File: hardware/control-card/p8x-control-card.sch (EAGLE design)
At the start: 34 parts, among them J1 DIN41612-96M, U1 CLK DIV, U10 UCODE ROM0, U11 UCODE ROM1, U12 UCODE ROM2, U13 UCODE ROM3, U14 PIPE0, U15 PIPE1, U16 PIPE2, U17 PIPE3, U18 STEP CNT, U2 74HCT14, U3 74HCT74, U4 74HCT00, U5 74HCT08, U6 74HCT32, U7 IR 74HCT377, U8 DLD DEC, U9 COND MUX, X1 4MHZ

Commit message: hw(rev B): control card — pipeline latches remapped to rev-B word
Phase 2, step 2. The 4x 74374 pipeline latches now map the 32-bit rev-B
control word: U15 gains PSEL2 (3-bit pointer select), ALUS3 moves to
U16, and U17 drives FCOND2/URST/HALT plus the new LDZN/SHCIN/SETC/CLRC.
The control card now drives PSEL2 (to reg-bank) and LDZN/SHCIN/SETC/CLRC
(to ALU) onto the backplane. Card retitled REV B; schematic regenerated,
validates clean.

Co-Authored-By: Claude Opus 4.8 <noreply@anthropic.com>
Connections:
- new net CLRC: J1.B27, U17.Q7
- new net LDZN: J1.C28, U17.Q4
- new net P17B2: U13.IO2, U17.D3
- new net P17B3: U13.IO3, U17.D4
- new net P17B4: U13.IO4, U17.D5
- new net P17B5: U13.IO5, U17.D6
- new net P17B6: U13.IO6, U17.D7
- new net PSEL2: J1.C27, U15.Q3
- new net SETC: J1.C30, U17.Q6
- new net SHCIN: J1.C29, U17.Q5
- net ALUM: now also U16.Q2; no longer U16.Q1
- net ALUS0: now also U15.Q6; no longer U15.Q5
- net ALUS1: now also U15.Q7; no longer U15.Q6
- net ALUS2: now also U15.Q8; no longer U15.Q7
- net ALUS3: now also U16.Q1; no longer U15.Q8
- net CIN: now also U16.Q3; no longer U16.Q2
- net FCOND0: now also U16.Q7; no longer U16.Q6
- net FCOND1: now also U16.Q8; no longer U16.Q7
- net FCOND2: now also U17.Q1; no longer U16.Q8
- net HALT: now also U17.Q3; no longer U17.Q2
- net LDF: now also U16.Q6; no longer U16.Q5
- net PDEC: now also U15.Q5; no longer U15.Q4
- net PINC: now also U15.Q4; no longer U15.Q3
- net SH0: now also U16.Q4; no longer U16.Q3
- net SH1: now also U16.Q5; no longer U16.Q4
- net URST: now also U17.Q2; no longer U17.Q1
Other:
- note added: "P8X CONTROL/MICROCODE CARD REV B"
- note removed: "P8X CONTROL/MICROCODE CARD REV A"

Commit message: hw: per-IC 100nF decoupling caps on every card
card standards sec.5 requires a decoupling cap per IC; only the backplane had
them. gen_eagle's card() now generates one 100nF cap (CDn, C_DISC footprint)
per IC on the five plug-in cards, placed next to its IC and wired VCC<->GND;
the memory card's separate build does the same for U1-U9.

Caps added: control 18, regbank 44, alu 31, io 15, cf 8, memory 9. All 7
boards regenerate with 0 validation errors; card schematic PDFs refreshed.
Placement is approximate (caps sit just below each IC) pending Fusion routing.

Clears a pre-fab blocker from the backlog.

Co-Authored-By: Claude Opus 4.8 <noreply@anthropic.com>
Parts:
- added CD1, CD10, CD11, CD12, CD13, CD14, CD15, CD16, CD17, CD18, CD2, CD3, CD4, CD5, CD6, CD7, CD8, CD9: 100N, p8x:CAP
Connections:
- net GND: now also CD1.2, CD10.2, CD11.2, CD12.2, CD13.2, CD14.2, CD15.2, CD16.2, CD17.2, CD18.2, CD2.2, CD3.2, CD4.2, CD5.2, CD6.2, CD7.2, CD8.2, CD9.2
- net VCC: now also CD1.1, CD10.1, CD11.1, CD12.1, CD13.1, CD14.1, CD15.1, CD16.1, CD17.1, CD18.1, CD2.1, CD3.1, CD4.1, CD5.1, CD6.1, CD7.1, CD8.1, CD9.1

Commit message: feat: 2nd ALU-input mux (rev C) — B-side operand can select T
Add a 2:1 mux on the ALU B-operand path so the second ALU operand can be
the T register instead of B, controlled by a new microcode-word bit.

- microcode (genucode.py): BSEL = word bit 31 (was the lone spare); new
  opcodes ADDT/SUBT/ANDT/ORT/XORT/CMPT (0x80-0x85) run the ALU with T as
  the B operand (B preserved); LDT #imm / LDT a (0x86/0x87) expose T, which
  was microcode-scratch-only and had no programmer-visible load.
- emulator (p8xemu.c): decode bit 31; ALU B operand = bsel ? T : B.
- hardware (gen_eagle.py): ALU card U32/U33 (74157 x2) mux BQ vs TQ -> 74181 B;
  BSEL latched in control-card pipe U17.Q8, carried on backplane B28 (was
  SPARE9). All 7 boards regenerate with 0 validation errors.
- bus map kept consistent across both generators (gen_eagle.py, gen_bus_pdf.py),
  the backplane render, and the hardware docs (bus-definition is authoritative).
- tests: new ISA coverage for the T-operand ops (sentinel wrong-operand bait);
  all 6 suites pass.
- docs: programmer's guide regenerated; BACKLOG updated (mux -> DONE; added a
  post-bringup idea to optimize monitor/OS/BASIC hot paths with the T ops).

Backward-compatible: no existing opcode changed; BSEL defaults 0 (= B register),
so existing monitor/OS/BASIC binaries are byte-identical.

Co-Authored-By: Claude Opus 4.8 <noreply@anthropic.com>
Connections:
- new net BSEL: J1.B28, U17.Q8
- new net P17B7: U13.IO7, U17.D8
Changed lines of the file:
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@@
 <label x="-22.86" y="-108.71" size="1.778" layer="95"/></segment>
+</net>
+<net name="P17B7" class="0">
+<segment><pinref part="U17" gate="G$1" pin="D8"/>
+<wire x1="122.22" y1="-543.56" x2="117.14" y2="-543.56" width="0.1524" layer="91"/>
+<label x="117.14" y="-543.05" size="1.778" layer="95"/></segment>
+<segment><pinref part="U13" gate="G$1" pin="IO7"/>
+<wire x1="157.78" y1="-398.78" x2="162.86" y2="-398.78" width="0.1524" layer="91"/>
+<label x="162.86" y="-398.27" size="1.778" layer="95"/></segment>
+</net>
+<net name="BSEL" class="0">
+<segment><pinref part="U17" gate="G$1" pin="Q8"/>
+<wire x1="157.78" y1="-538.48" x2="162.86" y2="-538.48" width="0.1524" layer="91"/>
+<label x="162.86" y="-537.97" size="1.778" layer="95"/></segment>
+<segment><pinref part="J1" gate="G$1" pin="B28"/>
+<wire x1="-17.78" y1="-111.76" x2="-22.86" y2="-111.76" width="0.1524" layer="91"/>
+<label x="-22.86" y="-111.25" size="1.778" layer="95"/></segment>
 </net>
 <net name="-USTL" class="0">

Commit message: feat: V flag + signed comparison branches (rev C)
Implement signed overflow (V) and signed-compare branches end to end, so the
machine can do signed ordering (C alone only gives unsigned).

Hardware (the old "one 7486 from carry-in vs carry-out of bit 7" plan was not
feasible: a 74181 4-bit group doesn't expose carry-into-bit-7). Sign-bit method:
  V = (A7 ^ F7) & (A7 ^ B7 ^ ~ALUS2)
  (B7 = muxed B operand, F7 = raw ALU result sign; isADD = ~S2). Ungated by M,
  so V is valid after ADD/SUB/CMP.
- ALU card: U34 (74HCT86) + U35 (74HCT08) derive V into the flag register
  (was tied low). FV already bused, no bus change.
- control card: U19 (74HCT86) -> N^V on cond-mux D6; spare U6 OR gate ->
  (N^V)|Z on D7 (both were grounded). FCOND 6/7 select them.

Microcode: BLT/BGE/BLE/BGT (0x44-0x47), FC LT=6 (N^V), LE=7 ((N^V)|Z).
Emulator: computes V by the identical Boolean; cond cases 6/7 added.
Tests: ISA coverage for sign-boundary cases unsigned C gets wrong (e.g. -128<1).
Docs: programmer's guide + BACKLOG (V flag VERIFY -> DONE).

All 7 boards regenerate with 0 validation errors; all 6 test suites pass.

Co-Authored-By: Claude Opus 4.8 <noreply@anthropic.com>
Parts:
- added CD19: 100N, p8x:CAP
- added U19: 74HCT86 NV-XOR, p8x:GATES14
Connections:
- new net NV: U19.1Y, U6.4A, U9.D6
- new net NVZ: U6.4Y, U9.D7
- net FN: now also U19.1A
- net FV: now also U19.1B
- net FZ: now also U6.4B
- net GND: now also CD19.2, U19.2A, U19.2B, U19.3A, U19.3B, U19.4A, U19.4B; no longer U6.4A, U6.4B, U9.D6, U9.D7
- net VCC: now also CD19.1
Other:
- moved on the sheet: C1, CD1, CD10, CD11, CD12, CD13, CD14, CD15, CD16, CD17, CD18, CD2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

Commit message: feat(hw): provision IRQ controller footprints (DNP) + reserve IRQ bus line
Per the chosen conservative path: add the interrupt-controller footprints and
the IRQ bus line so the controller can be built post-fab without a respin, but
WITHOUT the bus-critical logic that could brick an unvalidated board.

- Control card: U20 (74244 forcing buffer) + U21 (7474 IE/pending FF) placed as
  DNP. Safe connections wired: U20 inputs = $08 pattern, U20 !G tied high
  (outputs forced high-Z), IRQ line -> U21. Left UNWIRED (bus-critical, design
  with DRC first): U20 outputs onto the data bus, the enable/service sequencer,
  the EI/DI/RTI opcode decode, and the cross-card memory -RD suppression.
- Backplane: B29 = IRQ (was SPARE10), reserved; SPARE11 remains on B30.
- Bus map kept consistent across both generators + the backplane render + the
  three hardware docs (bus-definition is authoritative). Programmer's guide and
  BACKLOG updated.

All 7 boards regenerate with 0 validation errors; all 6 test suites pass.

Co-Authored-By: Claude Opus 4.8 <noreply@anthropic.com>
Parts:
- added CD20, CD21: 100N, p8x:CAP
- added U20: IRQ-FORCE DNP, p8x:74244
- added U21: IRQ/IE FF DNP, p8x:7474
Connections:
- new net IRQ: J1.B29, U21.1D
- net -RES: now also U21.!1CLR, U21.!2CLR
- net GND: now also CD20.2, CD21.2, U20.A1, U20.A2, U20.A3, U20.A5, U20.A6, U20.A7, U20.A8, U21.1CLK, U21.2CLK, U21.2D
- net VCC: now also CD20.1, CD21.1, U20.!G1, U20.!G2, U20.A4, U21.!1PRE, U21.!2PRE
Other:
- moved on the sheet: C1, CD1, CD10, CD11, CD12, CD13, CD14, CD15, CD16, CD17, CD18, CD19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

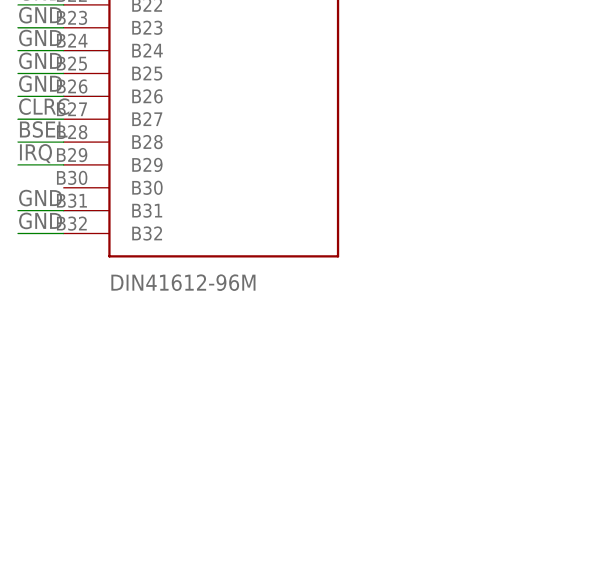
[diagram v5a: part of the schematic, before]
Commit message: fix(bom): card DIN connectors were undercounted (1 -> 6); label them FABC96R
Two fixes:
- card() built CARDS[name] from `allp`, which omitted J1 — so the 5 plug-in
  cards' DIN41612 edge connectors never reached the BOM (it showed qty 1, only
  the memory card's J1). Include J1 in allp (the schematic renderer already
  filters J1 by name, so rendering is unchanged). BOM now correctly shows 6 card
  connectors + 10 backplane receptacles.
- Card edge connector is FABC96R (user-specified): set the value label on every
  card J1 and name it in the BOM; backplane receptacles noted as the mating part.

Regenerated all boards + PDFs + BOM; all 6 test suites pass.

Co-Authored-By: Claude Opus 4.8 <noreply@anthropic.com>
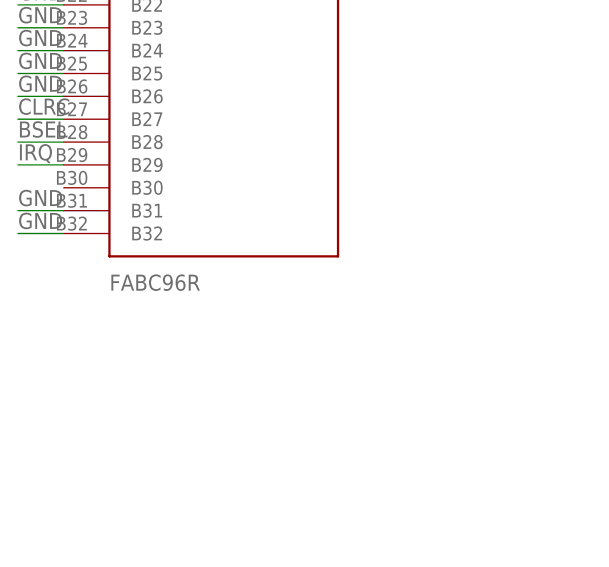
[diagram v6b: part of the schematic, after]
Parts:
- J1: value DIN41612-96M -> FABC96R
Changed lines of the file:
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@@
 <classes><class number="0" name="default" width="0" drill="0"/></classes>
 <parts>
-<part name="J1" library="p8x" deviceset="DIN96" device="" value="DIN41612-96M"/>
+<part name="J1" library="p8x" deviceset="DIN96" device="" value="FABC96R"/>
 <part name="U1" library="p8x" deviceset="74161" device="" value="CLK DIV"/>
 <part name="U2" library="p8x" deviceset="HEX14" device="" value="74HCT14"/>

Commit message: fix(hardware): connect IC power pins on the card()-built boards
Schematic-review fix. card() wired the edge-connector and decoupling-cap pins to
VCC/GND but never added each IC's own VCC/GND supply pin, so on control, regbank,
ALU, I/O, and CF the chips' power pads were not members of the power pours and
would not have been powered. (The hand-built memory card already did this; the
backplane has no ICs. validate() couldn't catch it — it checks pin-name legality,
not connectivity.)

- card(): append (ref,"VCC")/(ref,"GND") for every IC, skipping any pin already
  wired by hand (idempotent — avoids duplicate pinrefs, e.g. ALU U16 GND)
- regenerated all 7 boards (.sch/.brd), 0 validation errors
- board-level audit: every IC on every card now has both VCC and GND on the
  power signals
- BACKLOG: moved the critical item to DONE; theory docs' power-pin callouts
  updated to "fixed"

Co-Authored-By: Claude Opus 4.8 <noreply@anthropic.com>
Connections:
- net GND: now also U1.GND, U10.GND, U11.GND, U12.GND, U13.GND, U14.GND, U15.GND, U16.GND, U17.GND, U18.GND, U19.GND, U2.GND, U20.GND, U21.GND, U3.GND, U4.GND, U5.GND, U6.GND, U7.GND, U8.GND, U9.GND
- net VCC: now also U1.VCC, U10.VCC, U11.VCC, U12.VCC, U13.VCC, U14.VCC, U15.VCC, U16.VCC, U17.VCC, U18.VCC, U19.VCC, U2.VCC, U20.VCC, U21.VCC, U3.VCC, U4.VCC, U5.VCC, U6.VCC, U7.VCC, U8.VCC, U9.VCC
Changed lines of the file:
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@@
 <wire x1="122.22" y1="-1917.70" x2="117.14" y2="-1917.70" width="0.1524" layer="91"/>
 <label x="117.14" y="-1917.19" size="1.778" layer="95"/></segment>
+<segment><pinref part="U1" gate="G$1" pin="VCC"/>
+<wire x1="157.78" y1="25.40" x2="162.86" y2="25.40" width="0.1524" layer="91"/>
+<label x="162.86" y="25.91" size="1.778" layer="95"/></segment>
+<segment><pinref part="U2" gate="G$1" pin="VCC"/>
+<wire x1="259.38" y1="22.86" x2="264.46" y2="22.86" width="0.1524" layer="91"/>
+<label x="264.46" y="23.37" size="1.778" layer="95"/></segment>
+<segment><pinref part="U3" gate="G$1" pin="VCC"/>
+<wire x1="360.98" y1="27.94" x2="366.06" y2="27.94" width="0.1524" layer="91"/>
+<label x="366.06" y="28.45" size="1.778" layer="95"/></segment>
+<segment><pinref part="U4" gate="G$1" pin="VCC"/>
+<wire x1="462.58" y1="27.94" x2="467.66" y2="27.94" width="0.1524" layer="91"/>
+<label x="467.66" y="28.45" size="1.778" layer="95"/></segment>
+<segment><pinref part="U5" gate="G$1" pin="VCC"/>
+<wire x1="157.78" y1="-111.76" x2="162.86" y2="-111.76" width="0.1524" layer="91"/>
+<label x="162.86" y="-111.25" size="1.778" layer="95"/></segment>
+<segment><pinref part="U6" gate="G$1" pin="VCC"/>
+<wire x1="259.38" y1="-111.76" x2="264.46" y2="-111.76" width="0.1524" layer="91"/>
+<label x="264.46" y="-111.25" size="1.778" layer="95"/></segment>
+<segment><pinref part="U7" gate="G$1" pin="VCC"/>
+<wire x1="360.98" y1="-121.92" x2="366.06" y2="-121.92" width="0.1524" layer="91"/>
+<label x="366.06" y="-121.41" size="1.778" layer="95"/></segment>
+<segment><pinref part="U8" gate="G$1" pin="VCC"/>
+<wire x1="462.58" y1="-121.92" x2="467.66" y2="-121.92" width="0.1524" layer="91"/>
+<label x="467.66" y="-121.41" size="1.778" layer="95"/></segment>
+<segment><pinref part="U9" gate="G$1" pin="VCC"/>
+<wire x1="157.78" y1="-246.38" x2="162.86" y2="-246.38" width="0.1524" layer="91"/>
+<label x="162.86" y="-245.87" size="1.778" layer="95"/></segment>
+<segment><pinref part="U10" gate="G$1" pin="VCC"/>
+<wire x1="259.38" y1="-274.32" x2="264.46" y2="-274.32" width="0.1524" layer="91"/>
+<label x="264.46" y="-273.81" size="1.778" layer="95"/></segment>
+<segment><pinref part="U11" gate="G$1" pin="VCC"/>
+<wire x1="360.98" y1="-274.32" x2="366.06" y2="-274.32" width="0.1524" layer="91"/>
+<label x="366.06" y="-273.81" size="1.778" layer="95"/></segment>
+<segment><pinref part="U12" gate="G$1" pin="VCC"/>
+<wire x1="462.58" y1="-274.32" x2="467.66" y2="-274.32" width="0.1524" layer="91"/>
+<label x="467.66" y="-273.81" size="1.778" layer="95"/></segment>
+<segment><pinref part="U13" gate="G$1" pin="VCC"/>
+<wire x1="157.78" y1="-414.02" x2="162.86" y2="-414.02" width="0.1524" layer="91"/>
+<label x="162.86" y="-413.51" size="1.778" layer="95"/></segment>
+<segment><pinref part="U14" gate="G$1" pin="VCC"/>
+<wire x1="259.38" y1="-401.32" x2="264.46" y2="-401.32" width="0.1524" layer="91"/>
+<label x="264.46" y="-400.81" size="1.778" layer="95"/></segment>
+<segment><pinref part="U15" gate="G$1" pin="VCC"/>
+<wire x1="360.98" y1="-401.32" x2="366.06" y2="-401.32" width="0.1524" layer="91"/>
+<label x="366.06" y="-400.81" size="1.778" layer="95"/></segment>
+<segment><pinref part="U16" gate="G$1" pin="VCC"/>
+<wire x1="462.58" y1="-401.32" x2="467.66" y2="-401.32" width="0.1524" layer="91"/>
+<label x="467.66" y="-400.81" size="1.778" layer="95"/></segment>
+<segment><pinref part="U17" gate="G$1" pin="VCC"/>
+<wire x1="157.78" y1="-541.02" x2="162.86" y2="-541.02" width="0.1524" layer="91"/>
+<label x="162.86" y="-540.51" size="1.778" layer="95"/></segment>
+<segment><pinref part="U18" gate="G$1" pin="VCC"/>
+<wire x1="259.38" y1="-533.40" x2="264.46" y2="-533.40" width="0.1524" layer="91"/>
+<label x="264.46" y="-532.89" size="1.778" layer="95"/></segment>
+<segment><pinref part="U19" gate="G$1" pin="VCC"/>
+<wire x1="360.98" y1="-530.86" x2="366.06" y2="-530.86" width="0.1524" layer="91"/>
+<label x="366.06" y="-530.35" size="1.778" layer="95"/></segment>
+<segment><pinref part="U20" gate="G$1" pin="VCC"/>
+<wire x1="462.58" y1="-541.02" x2="467.66" y2="-541.02" width="0.1524" layer="91"/>
+<label x="467.66" y="-540.51" size="1.778" layer="95"/></segment>
+<segment><pinref part="U21" gate="G$1" pin="VCC"/>
+<wire x1="157.78" y1="-670.56" x2="162.86" y2="-670.56" width="0.1524" layer="91"/>
+<label x="162.86" y="-670.05" size="1.778" layer="95"/></segment>
 </net>
 <net name="GND" class="0">
@@
 <wire x1="157.78" y1="-1917.70" x2="162.86" y2="-1917.70" width="0.1524" layer="91"/>
 <label x="162.86" y="-1917.19" size="1.778" layer="95"/></segment>
+<segment><pinref part="U1" gate="G$1" pin="GND"/>
+<wire x1="157.78" y1="22.86" x2="162.86" y2="22.86" width="0.1524" layer="91"/>
+<label x="162.86" y="23.37" size="1.778" layer="95"/></segment>
+<segment><pinref part="U2" gate="G$1" pin="GND"/>
+<wire x1="259.38" y1="20.32" x2="264.46" y2="20.32" width="0.1524" layer="91"/>
+<label x="264.46" y="20.83" size="1.778" layer="95"/></segment>
+<segment><pinref part="U3" gate="G$1" pin="GND"/>
+<wire x1="360.98" y1="25.40" x2="366.06" y2="25.40" width="0.1524" layer="91"/>
+<label x="366.06" y="25.91" size="1.778" layer="95"/></segment>
+<segment><pinref part="U4" gate="G$1" pin="GND"/>
+<wire x1="462.58" y1="25.40" x2="467.66" y2="25.40" width="0.1524" layer="91"/>
+<label x="467.66" y="25.91" size="1.778" layer="95"/></segment>
+<segment><pinref part="U5" gate="G$1" pin="GND"/>
+<wire x1="157.78" y1="-114.30" x2="162.86" y2="-114.30" width="0.1524" layer="91"/>
+<label x="162.86" y="-113.79" size="1.778" layer="95"/></segment>
+<segment><pinref part="U6" gate="G$1" pin="GND"/>
+<wire x1="259.38" y1="-114.30" x2="264.46" y2="-114.30" width="0.1524" layer="91"/>
+<label x="264.46" y="-113.79" size="1.778" layer="95"/></segment>
+<segment><pinref part="U7" gate="G$1" pin="GND"/>
+<wire x1="360.98" y1="-124.46" x2="366.06" y2="-124.46" width="0.1524" layer="91"/>
+<label x="366.06" y="-123.95" size="1.778" layer="95"/></segment>
+<segment><pinref part="U8" gate="G$1" pin="GND"/>
+<wire x1="462.58" y1="-124.46" x2="467.66" y2="-124.46" width="0.1524" layer="91"/>
+<label x="467.66" y="-123.95" size="1.778" layer="95"/></segment>
+<segment><pinref part="U9" gate="G$1" pin="GND"/>
+<wire x1="157.78" y1="-248.92" x2="162.86" y2="-248.92" width="0.1524" layer="91"/>
+<label x="162.86" y="-248.41" size="1.778" layer="95"/></segment>
+<segment><pinref part="U10" gate="G$1" pin="GND"/>
+<wire x1="259.38" y1="-276.86" x2="264.46" y2="-276.86" width="0.1524" layer="91"/>
+<label x="264.46" y="-276.35" size="1.778" layer="95"/></segment>
+<segment><pinref part="U11" gate="G$1" pin="GND"/>
+<wire x1="360.98" y1="-276.86" x2="366.06" y2="-276.86" width="0.1524" layer="91"/>
+<label x="366.06" y="-276.35" size="1.778" layer="95"/></segment>
+<segment><pinref part="U12" gate="G$1" pin="GND"/>
+<wire x1="462.58" y1="-276.86" x2="467.66" y2="-276.86" width="0.1524" layer="91"/>
+<label x="467.66" y="-276.35" size="1.778" layer="95"/></segment>
+<segment><pinref part="U13" gate="G$1" pin="GND"/>
+<wire x1="157.78" y1="-416.56" x2="162.86" y2="-416.56" width="0.1524" layer="91"/>
+<label x="162.86" y="-416.05" size="1.778" layer="95"/></segment>
+<segment><pinref part="U14" gate="G$1" pin="GND"/>
+<wire x1="259.38" y1="-403.86" x2="264.46" y2="-403.86" width="0.1524" layer="91"/>
+<label x="264.46" y="-403.35" size="1.778" layer="95"/></segment>
+<segment><pinref part="U15" gate="G$1" pin="GND"/>
+<wire x1="360.98" y1="-403.86" x2="366.06" y2="-403.86" width="0.1524" layer="91"/>
+<label x="366.06" y="-403.35" size="1.778" layer="95"/></segment>
+<segment><pinref part="U16" gate="G$1" pin="GND"/>
+<wire x1="462.58" y1="-403.86" x2="467.66" y2="-403.86" width="0.1524" layer="91"/>
+<label x="467.66" y="-403.35" size="1.778" layer="95"/></segment>
+<segment><pinref part="U17" gate="G$1" pin="GND"/>
+<wire x1="157.78" y1="-543.56" x2="162.86" y2="-543.56" width="0.1524" layer="91"/>
+<label x="162.86" y="-543.05" size="1.778" layer="95"/></segment>
+<segment><pinref part="U18" gate="G$1" pin="GND"/>
+<wire x1="259.38" y1="-535.94" x2="264.46" y2="-535.94" width="0.1524" layer="91"/>
+<label x="264.46" y="-535.43" size="1.778" layer="95"/></segment>
+<segment><pinref part="U19" gate="G$1" pin="GND"/>
+<wire x1="360.98" y1="-533.40" x2="366.06" y2="-533.40" width="0.1524" layer="91"/>
+<label x="366.06" y="-532.89" size="1.778" layer="95"/></segment>
+<segment><pinref part="U20" gate="G$1" pin="GND"/>
+<wire x1="462.58" y1="-543.56" x2="467.66" y2="-543.56" width="0.1524" layer="91"/>
+<label x="467.66" y="-543.05" size="1.778" layer="95"/></segment>
+<segment><pinref part="U21" gate="G$1" pin="GND"/>
+<wire x1="157.78" y1="-673.10" x2="162.86" y2="-673.10" width="0.1524" layer="91"/>
+<label x="162.86" y="-672.59" size="1.778" layer="95"/></segment>
 </net>
 <net name="RUNSW" class="0">
